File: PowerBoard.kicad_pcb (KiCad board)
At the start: 2 copper layers, 50 x 60 mm, 73 parts, among them Q3 PSMN020-100YS, Q4 PSMN020-100YS, U12 TPS16851VMAR, U13 LM5050-1, U14 TPS16851VMAR, U15 LM5050-1

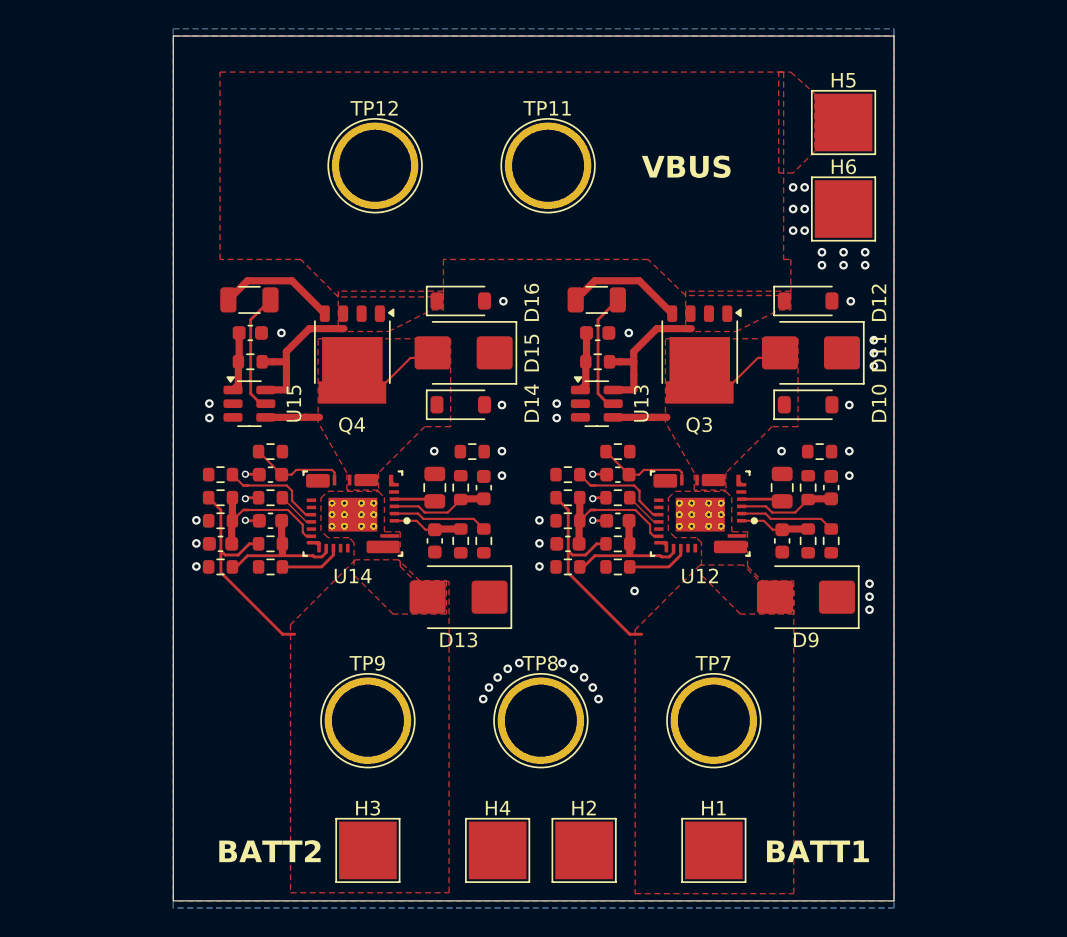
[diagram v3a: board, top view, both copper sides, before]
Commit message: Finished layout for load switch dev board.
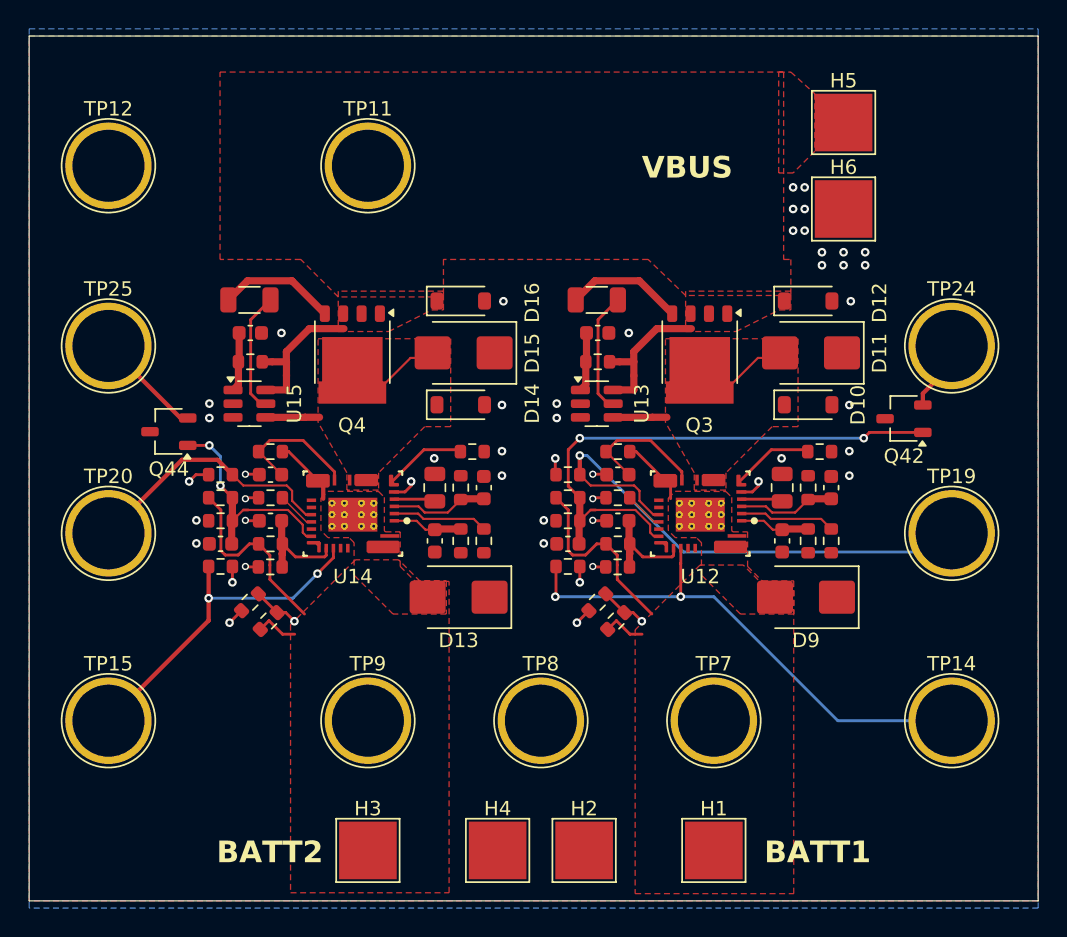
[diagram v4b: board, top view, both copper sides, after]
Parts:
- added Q42: 2N7002 TR PBFREE, Package_TO_SOT_SMD:TSOT-23, F.Cu at (173.7, 99.0)
- added Q44: 2N7002 TR PBFREE, Package_TO_SOT_SMD:TSOT-23, F.Cu at (122.7, 100.0)
- added R110: 33k, Resistor_SMD:R_0603_1608Metric, F.Cu at (153.7, 113.1)
- added R111: 33k, Resistor_SMD:R_0603_1608Metric, F.Cu at (129.6, 113.1)
- added R115: 8.16k, Resistor_SMD:R_0603_1608Metric, F.Cu at (152.4, 111.8)
- added R116: 8.16k, Resistor_SMD:R_0603_1608Metric, F.Cu at (128.3, 111.8)
- added TP14: TP_PGOOD, TestPoint:TestPoint_Plated_Hole_D5.0mm, F.Cu at (177.0, 120.0)
- added TP15: TP_PGOOD, TestPoint:TestPoint_Plated_Hole_D5.0mm, F.Cu at (118.5, 120.0)
- added TP19: TP_FLTn, TestPoint:TestPoint_Plated_Hole_D5.0mm, F.Cu at (177.0, 107.0)
- added TP20: TP_FLTn, TestPoint:TestPoint_Plated_Hole_D5.0mm, F.Cu at (118.5, 107.0)
- added TP24: TP_PGOOD, TestPoint:TestPoint_Plated_Hole_D5.0mm, F.Cu at (177.0, 94.0)
- added TP25: TP_PGOOD, TestPoint:TestPoint_Plated_Hole_D5.0mm, F.Cu at (118.5, 94.0)
- moved TP12 18.5 mm to (118.5, 81.5)
- moved TP11 12.5 mm to (136.5, 81.5)
- moved R45 3.47 mm to (150.4, 109.3), turned to 0 degrees
- moved R58 3.47 mm to (126.3, 109.3), turned to 0 degrees
- moved R40 3.45 mm to (153.8, 109.3)
- moved R53 3.45 mm to (129.7, 109.3)
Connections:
- net Net-(D10-A2) renamed /Main/batt1_load_sw/BUS
- net Net-(D14-A2) renamed /Main/batt2_load_sw/BUS
- net Net-(U12-EN_UVLO) renamed /Main/batt1_load_sw/EN_UVLO
- net Net-(U14-EN_UVLO) renamed /Main/batt2_load_sw/EN_UVLO
- R45 pad 2: +5V -> /Main/batt1_load_sw/V_PULLUP
- R46 pad 2: +5V -> /Main/batt1_load_sw/V_PULLUP
- R58 pad 2: +5V -> /Main/batt2_load_sw/V_PULLUP
- R59 pad 2: +5V -> /Main/batt2_load_sw/V_PULLUP
- U12 pad 20: /Main/BATT1.EN -> unconnected-(U12-SWEN-Pad20)
- U14 pad 20: /Main/BATT2.EN -> unconnected-(U14-SWEN-Pad20)
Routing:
- net /Main/BATT1.PGOOD: track 4.36 -> 36.6 mm, vias 0 -> 2
- net /Main/BATT1.FLTn: track 7.04 -> 37.5 mm, vias 0 -> 1
- net /Main/batt1_load_sw/EN_UVLO: track 10.0 -> 38.8 mm, vias 0 -> 2
- net /Main/BATT2.PGOOD: track 4.36 -> 24.1 mm, vias 0 -> 2
- net /Main/BATT2.FLTn: track 7.04 -> 18.2 mm
- net GND: track 5.81 -> 13.5 mm, vias 57 -> 44
- net /Main/BATT2.EN: track 0.00 -> 7.57 mm
- net /Main/batt2_load_sw/V_PULLUP: track 0.00 -> 5.93 mm, vias 0 -> 3
- net /Main/batt2_load_sw/EN_UVLO: track 10.0 -> 15.8 mm, vias 0 -> 2
- net Net-(U12-SFT_SEL): track 0.00 -> 5.78 mm
- net Net-(U14-SFT_SEL): track 0.00 -> 5.78 mm
- net /Main/batt1_load_sw/V_PULLUP: track 0.00 -> 5.54 mm, vias 0 -> 3
- net /Main/batt1_load_sw/IN: track 15.8 -> 21.3 mm
- net /Main/batt2_load_sw/IN: track 15.8 -> 21.3 mm
- net /Main/BATT1.EN: track 0.00 -> 4.93 mm
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- added copper zone on In2.Cu, net /Main/batt1_load_sw/V_PULLUP
- added copper zone on In2.Cu, net /Main/batt2_load_sw/V_PULLUP
- added copper zone on In1.Cu, net GND
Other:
- board size 50 x 60 mm -> 70 x 60 mm
- copper layers 2 -> 4

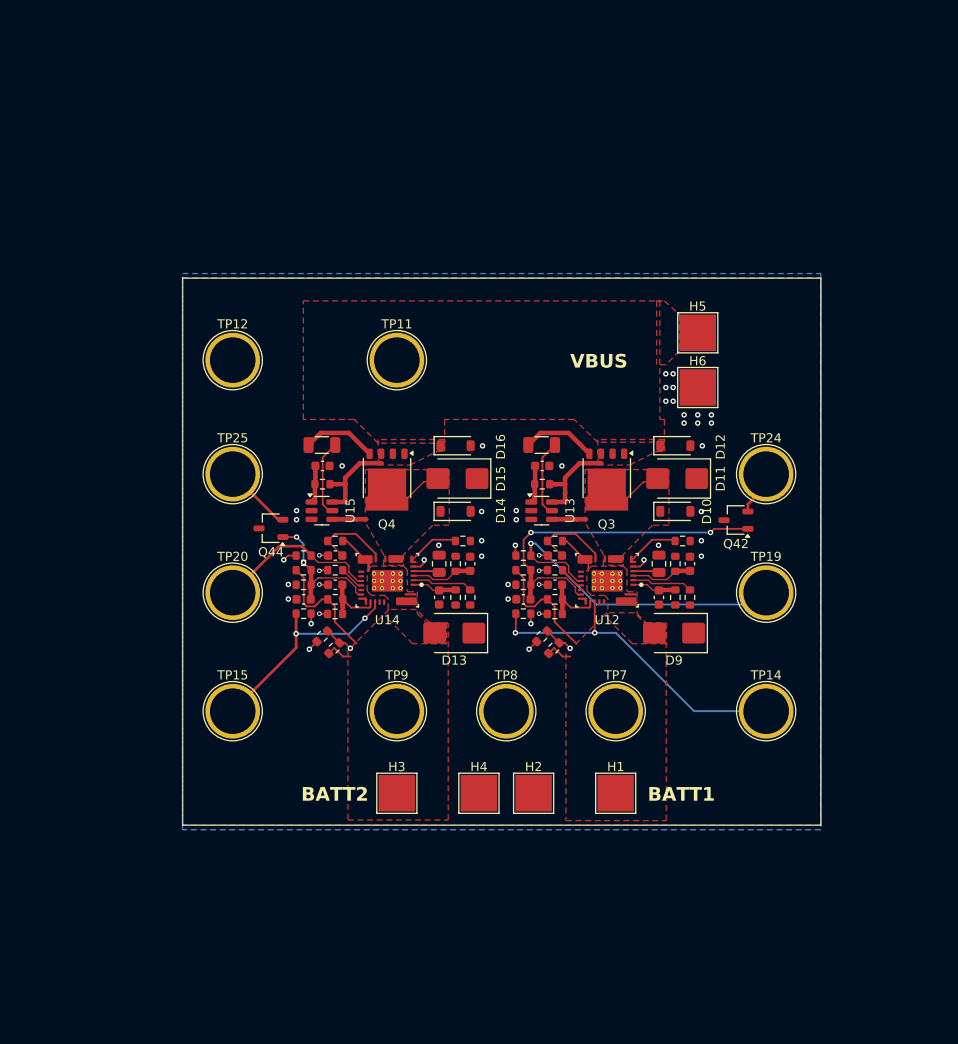
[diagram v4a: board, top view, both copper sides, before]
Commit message: Removing pads and adding more TPs and also mounting holes
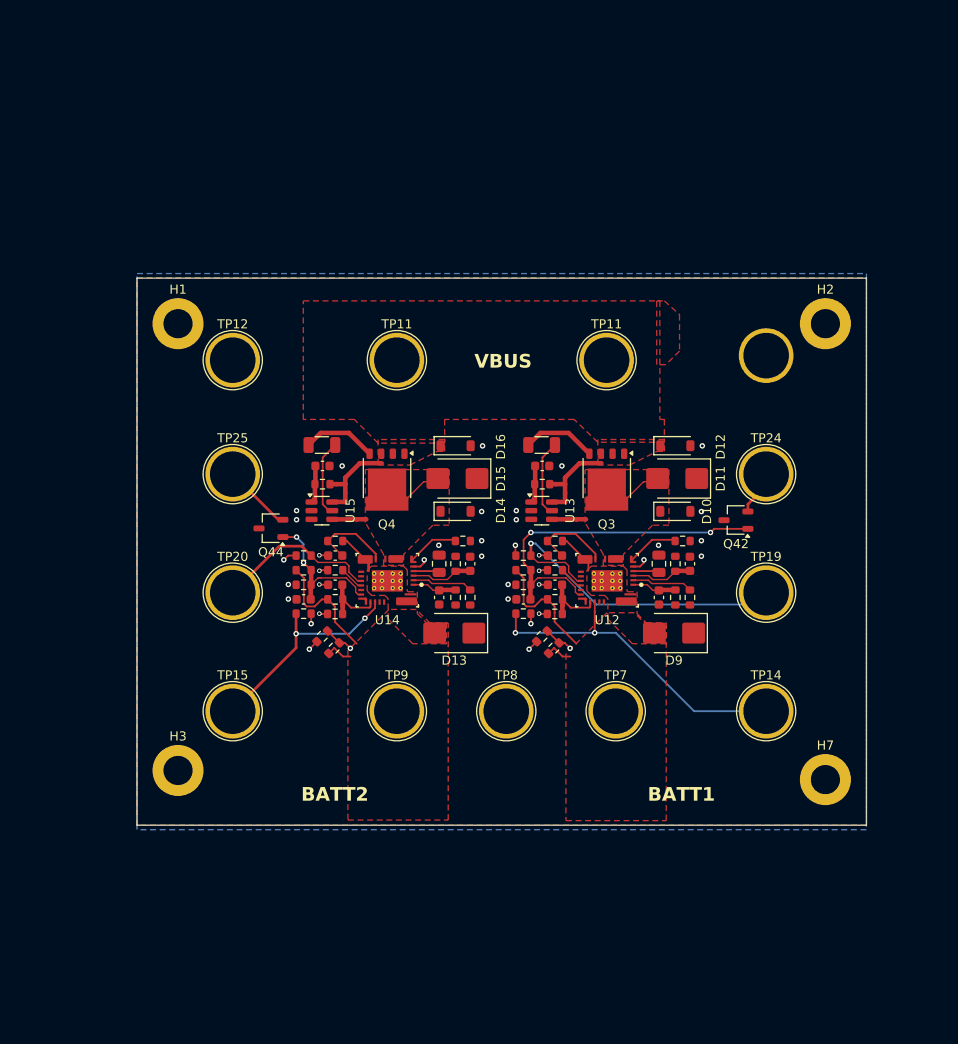
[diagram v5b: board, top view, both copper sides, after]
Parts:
- removed H4, H5, H6: MountingHole_Pad_MP, TestPoint:TestPoint_Pad_4.0x4.0mm
- added ?: , , F.Cu at (177.0, 81.0)
- added H7: MountingHole, MountingHole:MountingHole_3.2mm_M3_DIN965_Pad, F.Cu at (183.5, 127.5)
- added TP11: BATT2_DRV_RTN, TestPoint:TestPoint_Plated_Hole_D5.0mm, F.Cu at (159.5, 81.5)
- H1, H2, H3: value MountingHole_Pad_MP -> MountingHole; footprint TestPoint:TestPoint_Pad_4.0x4.0mm -> MountingHole:MountingHole_3.2mm_M3_DIN965_Pad
- R47, R60: value 1.26k -> 27.4k
- R48, R61: value 464 -> 10k
- R49, R62: value 1k -> 220k
- moved H1 70.4 mm to (112.5, 77.5)
- moved H2 60.6 mm to (183.5, 77.5)
- moved H3 24.1 mm to (112.5, 126.5)
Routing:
- net GND: vias 44 -> 32
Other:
- board size 70 x 60 mm -> 80 x 60 mm

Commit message: Finishing up layout
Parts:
- added G***: LOGO, LOGO, F.Cu at (184.4, 102.9)
- added G***: LOGO, LOGO, F.Cu at (148.0, 80.0)
- R47, R60: value 27.4k -> 5.49k
- R48, R61: value 10k -> 2k
- R49, R62: value 220k -> 44.8k
- moved NT12 4.25 mm to (126.1, 95.1), turned to 180 degrees
- moved NT9 4.25 mm to (150.2, 95.1), turned to 180 degrees
- moved TP14 4.00 mm to (177.0, 124.0)
- moved TP15 4.00 mm to (118.5, 124.0)
- moved TP7 4.00 mm to (160.5, 124.0)
- moved TP8 4.00 mm to (148.5, 124.0)
- moved TP9 4.00 mm to (136.5, 124.0)
- moved NT11 3.98 mm to (126.9, 96.1), turned to 180 degrees
- moved NT8 3.98 mm to (151.0, 96.1), turned to 180 degrees
- moved TP19 2.83 mm to (177.0, 109.8)
- moved TP20 2.83 mm to (118.5, 109.8)
- moved Q3 2.43 mm to (159.5, 92.0), turned to 90 degrees
- moved Q4 2.43 mm to (135.4, 92.0), turned to 90 degrees
- moved Q42 1.95 mm to (173.7, 101.0)
- moved TP24 1.67 mm to (177.0, 95.7)
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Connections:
- Q3 pad D: /Main/batt1_load_sw/BUS -> VBUS
- Q3 pad S: VBUS -> /Main/batt1_load_sw/BUS
- Q4 pad D: /Main/batt2_load_sw/BUS -> VBUS
- Q4 pad S: VBUS -> /Main/batt2_load_sw/BUS
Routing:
- net /Main/batt1_load_sw/V_PULLUP: track 5.54 -> 16.6 mm, vias 3 -> 2
- net /Main/batt2_load_sw/V_PULLUP: track 5.93 -> 16.6 mm, vias 3 -> 2
- net /Main/batt2_load_sw/BUS: track 5.67 -> 0.00 mm
- net /Main/batt1_load_sw/BUS: track 5.67 -> 0.00 mm
- net /Main/BATT2.PGOOD: track 24.1 -> 29.7 mm
- net VBUS: track 12.6 -> 17.9 mm
- net /Main/BATT2.FLTn: track 18.2 -> 22.9 mm, vias 0 -> 1
- net /Main/BATT1.EN: track 4.93 -> 9.34 mm
- net Net-(U15-VS): track 4.13 -> 7.70 mm, vias 0 -> 2
- net Net-(U13-VS): track 4.13 -> 7.70 mm, vias 0 -> 2
- net Net-(U13-GATE): track 8.41 -> 11.0 mm
- net Net-(U15-GATE): track 8.41 -> 11.0 mm
- net /Main/BATT1.PGOOD: track 36.6 -> 38.3 mm
- net Net-(Q3-PadG): track 8.19 -> 9.53 mm
- net Net-(Q4-PadG): track 8.19 -> 9.53 mm
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- added copper zone on In2.Cu, net GND
- removed copper zone on In2.Cu, net /Main/batt1_load_sw/V_PULLUP
- removed copper zone on In2.Cu, net /Main/batt2_load_sw/V_PULLUP
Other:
- board text added: "BATT1.EN"
- board text added: "BATT1.FLTn"
- board text added: "BATT1.IN"
- board text added: "BATT1.PGOOD"
- board text added: "BATT2.EN"
- board text added: "BATT2.FLTn"
- board text added: "BATT3.PGOOD"
- board text added: "Ezzat Suhaime"
- board text added: "GND"
- board text added: "LSW DEV"

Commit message: Touching up the baord
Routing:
- net GND: vias 28 -> 38
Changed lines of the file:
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@@
+	)
+	(via
+		(at 156.3 110.3)
+		(size 0.6)
+		(drill 0.4)
+		(layers "F.Cu" "B.Cu")
+		(free yes)
+		(net 1)
 	)
 	(via
@@
 		(size 0.6)
 		(drill 0.3)
+		(layers "F.Cu" "B.Cu")
+		(free yes)
+		(net 1)
+	)
+	(via
+		(at 131.6 96)
+		(size 0.6)
+		(drill 0.4)
 		(layers "F.Cu" "B.Cu")
 		(free yes)
@@
 	)
 	(via
+		(at 155.8 96)
+		(size 0.6)
+		(drill 0.4)
+		(layers "F.Cu" "B.Cu")
+		(free yes)
+		(net 1)
+	)
+	(via
 		(at 152.1 109.3)
 		(size 0.5)
@@
 	)
 	(via
+		(at 147.5 95)
+		(size 0.6)
+		(drill 0.3)
+		(layers "F.Cu" "B.Cu")
+		(free yes)
+		(net 1)
+	)
+	(via
 		(at 126.9 113.2)
 		(size 0.6)
@@
 		(size 0.6)
 		(drill 0.3)
+		(layers "F.Cu" "B.Cu")
+		(free yes)
+		(net 1)
+	)
+	(via
+		(at 155.8 90)
+		(size 0.6)
+		(drill 0.4)
+		(layers "F.Cu" "B.Cu")
+		(free yes)
+		(net 1)
+	)
+	(via
+		(at 132.1 110.2)
+		(size 0.6)
+		(drill 0.4)
 		(layers "F.Cu" "B.Cu")
 		(free yes)
@@
 	)
 	(via
+		(at 171.7 95)
+		(size 0.6)
+		(drill 0.3)
+		(layers "F.Cu" "B.Cu")
+		(free yes)
+		(net 1)
+	)
+	(via
 		(at 139.5 103.4)
 		(size 0.6)
@@
 	(via
 		(at 165.2 101.8)
+		(size 0.6)
+		(drill 0.3)
+		(layers "F.Cu" "B.Cu")
+		(free yes)
+		(net 1)
+	)
+	(via
+		(at 171.7 94)
 		(size 0.6)
 		(drill 0.3)
@@
 	)
 	(via
+		(at 147.5 94)
+		(size 0.6)
+		(drill 0.3)
+		(layers "F.Cu" "B.Cu")
+		(free yes)
+		(net 1)
+	)
+	(via
 		(at 163.6 103.4)
 		(size 0.6)
@@
 		(size 0.6)
 		(drill 0.3)
+		(layers "F.Cu" "B.Cu")
+		(free yes)
+		(net 1)
+	)
+	(via
+		(at 131.6 90)
+		(size 0.6)
+		(drill 0.4)
 		(layers "F.Cu" "B.Cu")
 		(free yes)
@@
 			(thermal_bridge_width 0.5)
 			(island_removal_mode 2)
-			(island_area_min 20)
+			(island_area_min 5)
 		)
 		(polygon

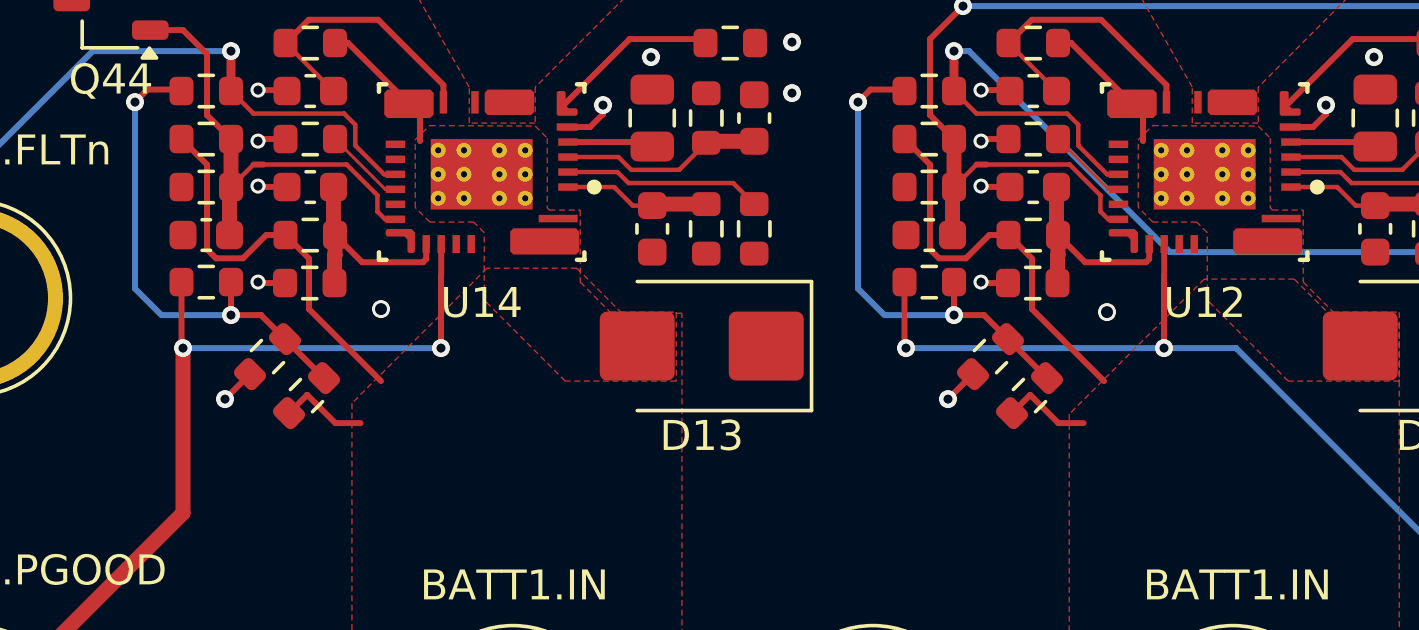
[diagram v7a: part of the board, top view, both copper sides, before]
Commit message: n+1 board shipment, moving vias off BATT_IN planes
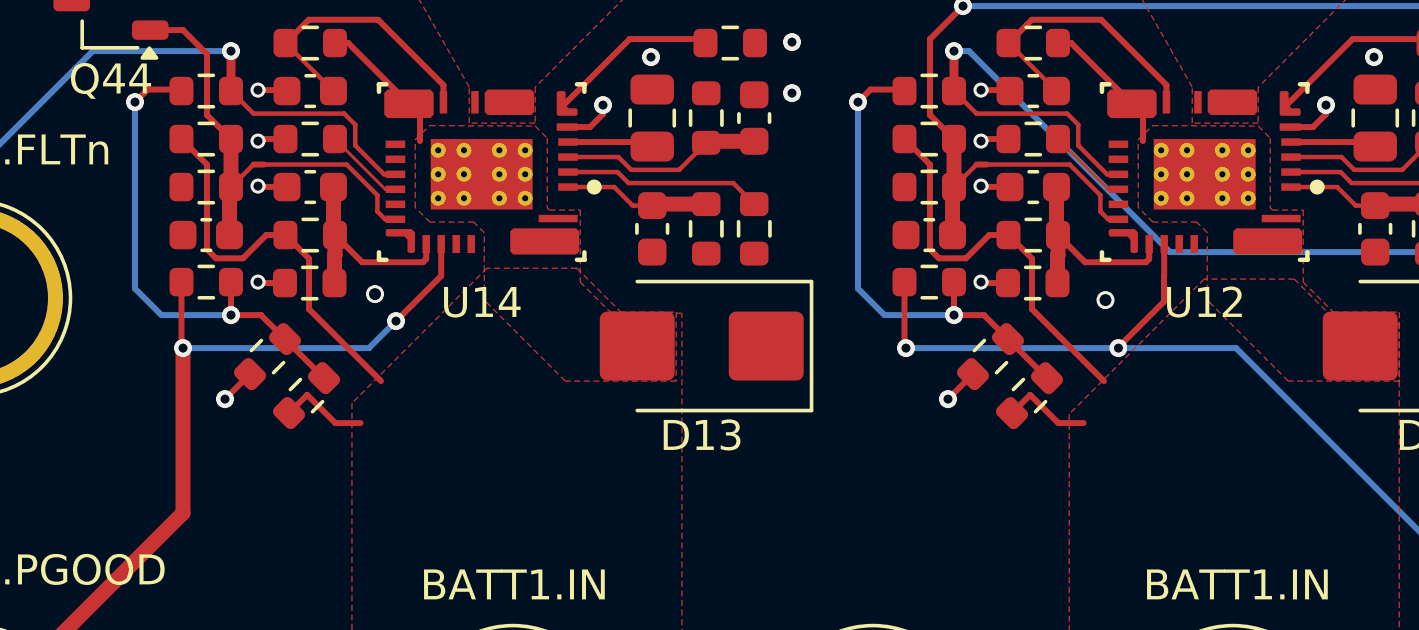
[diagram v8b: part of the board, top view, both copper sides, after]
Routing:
- net /Main/BATT2.PGOOD: track 29.7 -> 28.3 mm
- net /Main/BATT1.PGOOD: track 38.3 -> 38.9 mm
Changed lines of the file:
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@@
 	)
 	(via
-		(at 156.3 110.3)
+		(at 156.25 109.9)
 		(size 0.6)
 		(drill 0.4)
@@
 	)
 	(via
-		(at 132.1 110.2)
-		(size 0.6)
-		(drill 0.4)
-		(layers "F.Cu" "B.Cu")
-		(free yes)
-		(net 1)
-	)
-	(via
 		(at 152.1 104.6)
 		(size 0.5)
@@
 		(drill 0.3)
 		(layers "F.Cu" "B.Cu")
+		(net 1)
+	)
+	(via
+		(at 131.9 109.7)
+		(size 0.6)
+		(drill 0.4)
+		(layers "F.Cu" "B.Cu")
+		(free yes)
 		(net 1)
 	)
@@
 	)
 	(segment
+		(start 156.681029 111.5)
+		(end 156.681029 111.468971)
+		(width 0.2)
+		(layer "F.Cu")
+		(net 22)
+	)
+	(segment
+		(start 158.2 109.95)
+		(end 158.2 109.1)
+		(width 0.2)
+		(layer "F.Cu")
+		(net 22)
+	)
+	(segment
 		(start 149.6 111.4)
 		(end 149.55 111.35)
@@
 	)
 	(segment
-		(start 158.2 111.5)
-		(end 158.2 109.1)
-		(width 0.2)
-		(layer "F.Cu")
-		(net 22)
-	)
-	(segment
 		(start 158.206446 109.093554)
 		(end 158.206446 108.03175)
@@
 	)
 	(segment
+		(start 156.681029 111.468971)
+		(end 158.2 109.95)
+		(width 0.2)
+		(layer "F.Cu")
+		(net 22)
+	)
+	(segment
 		(start 149.6 111.5)
 		(end 149.6 111.4)
@@
 	)
 	(via
-		(at 158.2 111.5)
+		(at 156.681029 111.5)
 		(size 0.6)
 		(drill 0.3)
@@
 	)
 	(segment
-		(start 158.2 111.5)
-		(end 160.6 111.5)
+		(start 173.1 124)
+		(end 177 124)
 		(width 0.2)
 		(layer "B.Cu")
@@
 	)
 	(segment
+		(start 156.681029 111.5)
+		(end 149.6 111.5)
+		(width 0.2)
+		(layer "B.Cu")
+		(net 22)
+	)
+	(segment
 		(start 160.6 111.5)
 		(end 173.1 124)
@@
 	)
 	(segment
-		(start 149.6 111.5)
-		(end 158.2 111.5)
+		(start 156.681029 111.5)
+		(end 160.6 111.5)
 		(width 0.2)
 		(layer "B.Cu")
@@
 	)
 	(segment
-		(start 173.1 124)
-		(end 177 124)
-		(width 0.2)
-		(layer "B.Cu")
-		(net 22)
-	)
-	(segment
 		(start 156.681445 105.706751)
 		(end 156.302482 105.706751)
@@
 	)
 	(segment
+		(start 132.6 110.6)
+		(end 134.106446 109.093554)
+		(width 0.2)
+		(layer "F.Cu")
+		(net 29)
+	)
+	(segment
 		(start 125.45 111.35)
 		(end 125.45 109.3)
@@
 	)
 	(segment
-		(start 134.1 109.1)
-		(end 134.106446 109.093554)
-		(width 0.2)
-		(layer "F.Cu")
-		(net 29)
-	)
-	(segment
 		(start 125.5 111.5)
 		(end 125.5 117)
@@
 	)
 	(segment
-		(start 134.1 111.5)
-		(end 134.1 109.1)
-		(width 0.2)
-		(layer "F.Cu")
-		(net 29)
-	)
-	(segment
 		(start 125.5 111.5)
 		(end 125.5 111.4)
@@
 	)
 	(via
-		(at 134.1 111.5)
+		(at 132.6 110.6)
 		(size 0.6)
 		(drill 0.3)
@@
 	)
 	(segment
+		(start 131.7 111.5)
+		(end 132.6 110.6)
+		(width 0.2)
+		(layer "B.Cu")
+		(net 29)
+	)
+	(segment
 		(start 125.5 111.5)
-		(end 134.1 111.5)
+		(end 131.7 111.5)
 		(width 0.2)
 		(layer "B.Cu")
